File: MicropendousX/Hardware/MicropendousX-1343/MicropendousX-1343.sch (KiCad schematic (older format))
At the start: 92 parts, among them IC1 LPC1343, P1 Bottom, P2 Top, Q1 NCH, SW1 RESET, SW2 MSC, U1 microSD, U2 USBCONN, U3 CORTEX_M3_JTAG, U4 1117-3.3, X1 12MHz

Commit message: Updated MicropendousX-1343 hardware design
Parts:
- removed Q1: NCH, symbol MOSFET_N_OPENDOUS
- added C9: 10u, symbol C_MINI
- added Q1: PCH, symbol MOSFET_P_OPENDOUS
- C8: value 10n -> 10u
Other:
- note added: "BSS84"
- note removed: "2N7002"

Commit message: Updated MicropendousX-1343 and KiCAD Schematic Symbol Library
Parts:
- removed U3: CORTEX_M3_JTAG, symbol CONN_CORTEXM3_JTAG
- removed V10, V21, V22, V23, V44: VIA, symbol VIA
- added R7: 0, symbol R_MINI
- added U3: SWD JTAG, symbol CONN_CORTEX_DEBUG
- added V65, V66, V67: VIA, symbol VIA
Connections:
- net labels added: PIO0_11-AD0-CT32B0_MAT3, PIO1_0-AD1-CT32B_CAP0, PIO1_1-AD2-CT32B1_MAT0, PIO1_2-AD3-CT32B1_MAT1, SWCLK-PIO0_10-SCK-CT16B0_MAT2, SWDIO-PIO1_3-AD4-CT32B1_MAT2, SWO
- net labels removed: PIO1_3-SWDIO-AD4-CT32B1_MAT2, TCK-SWCLK, TDI, TDO, TMS, nTRST
- no-connect marks 3 -> 4
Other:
- note added: "Cortex Debug Connector"
- note added: "LPC1??? are SWD-Debug Only"
- note added: "Optional"
- moved on the sheet: P1, P2, V11, V12, V13, V14, V20, V41, V42, V43, V57, V58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

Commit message: Updated hardware designs. Added Blinky demos with and without assembly.
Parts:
- U4: value 1117-3.3 -> 1117
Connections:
- wire segments 148 -> 152
- no-connect marks 4 -> 5
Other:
- note added: "LPC1343 is SWD-Debug Only"
- note added: "This allows the board to be used with the non-USB QFP48 LPC13?? and LPC11?? ICs"
- note removed: "LPC1??? are SWD-Debug Only"
- note removed: "This allows the board to be used with the non-USB QFP48 LPC1??? ICs"
- moved on the sheet: P1, P2

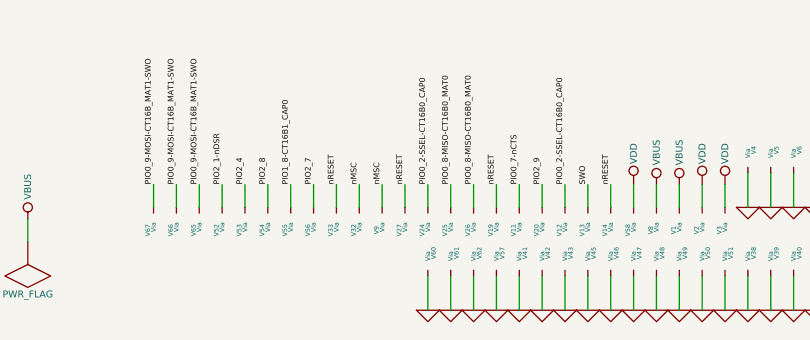
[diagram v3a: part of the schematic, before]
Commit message: Updated MicropendousX-1343 to a better stocked microSD connector (Amphenol 101-00303).
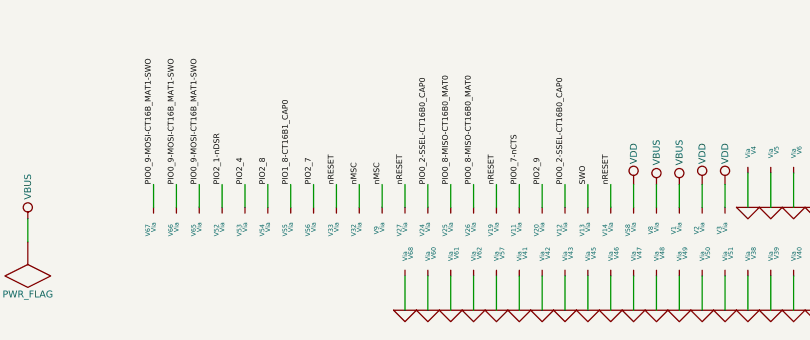
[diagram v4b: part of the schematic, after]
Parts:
- added V68: VIA, symbol VIA
- CR1, CR2: value ESD_ZENER -> ESD
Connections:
- wire segments 152 -> 153
